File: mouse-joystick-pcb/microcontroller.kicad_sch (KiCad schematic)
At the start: 1 part

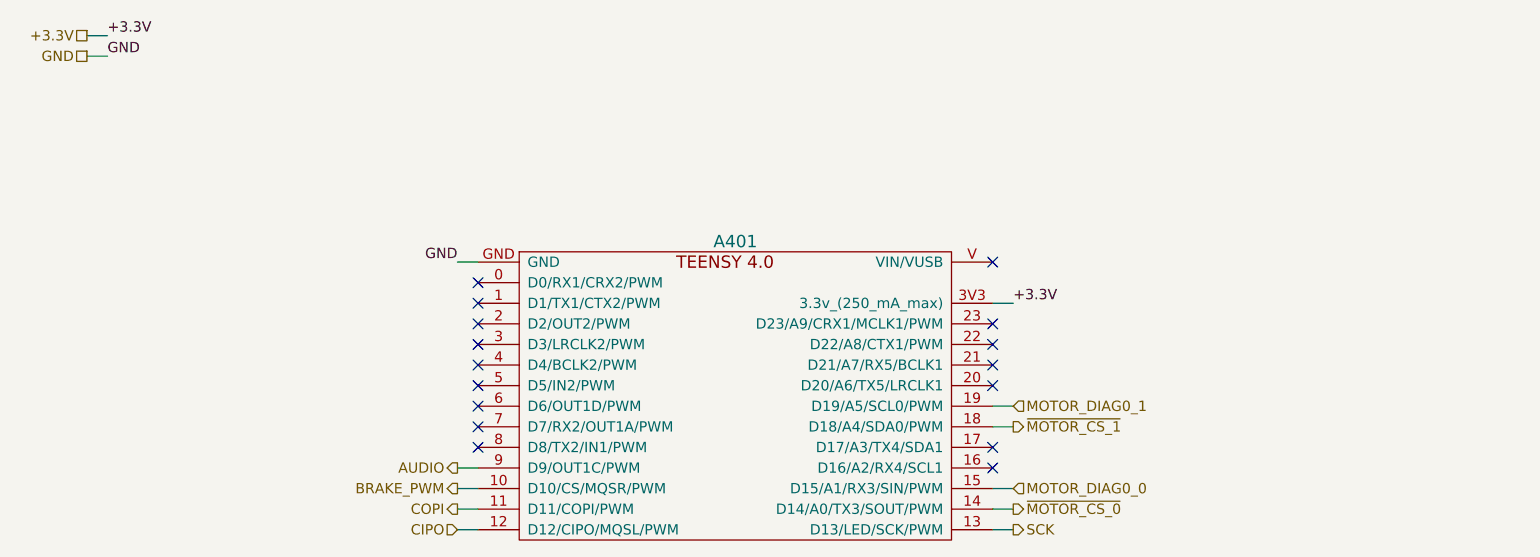
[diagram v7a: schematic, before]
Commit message: Add torque-sensor sheet
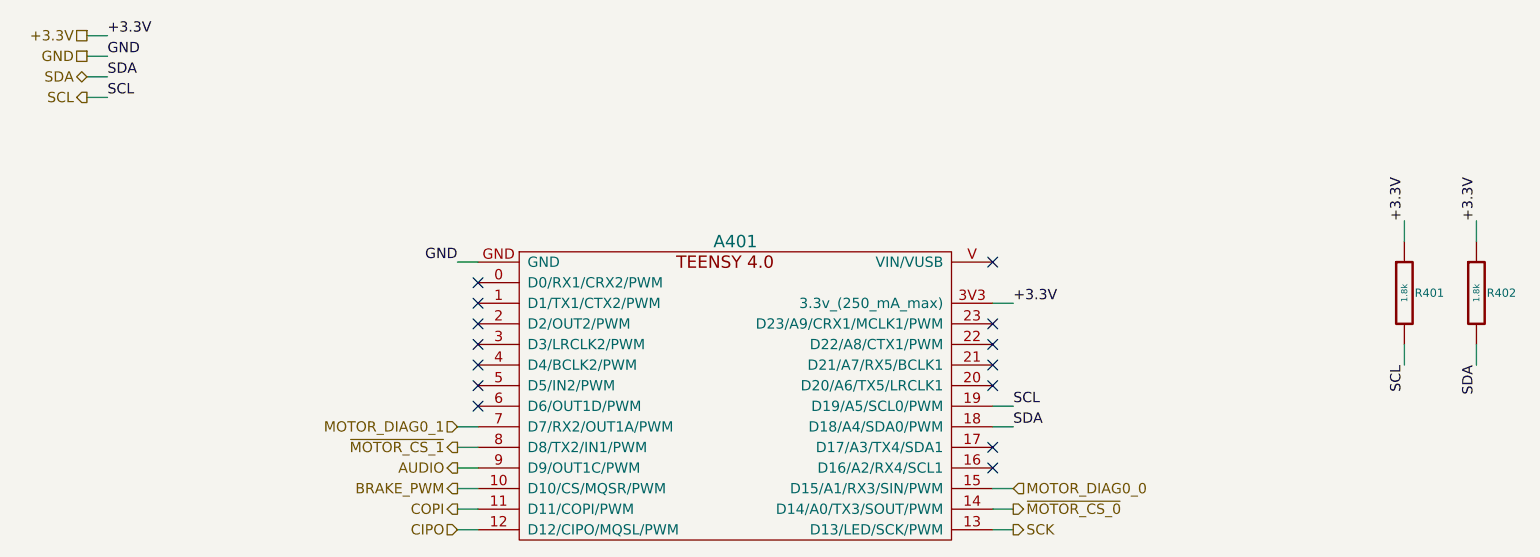
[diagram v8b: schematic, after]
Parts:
- added R401, R402: 1.8k, Janelia:R_0402_1005Metric, symbol Janelia:R_1.8k_0402
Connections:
- net +3.3V: now also R401.1, R402.1
- net MOTOR_DIAG0_1: now also A401.7 (D7/RX2/OUT1A/PWM); no longer A401.19 (D19/A5/SCL0/PWM)
- net ~{MOTOR_CS_1}: now also A401.8 (D8/TX2/IN1/PWM); no longer A401.18 (D18/A4/SDA0/PWM)
- new net SCL: A401.19 (D19/A5/SCL0/PWM), R401.2
- new net SDA: A401.18 (D18/A4/SDA0/PWM), R402.2
- no-connect marks 16 -> 14
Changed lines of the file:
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@@
   (title_block
     (title "mouse-joystick-pcb")
-    (date "2024-10-09")
+    (date "2024-10-11")
     (rev "1.0")
     (company "Peter Polidoro")
@@
   (no_connect (at 162.56 92.71))
   (no_connect (at 162.56 90.17))
-  (no_connect (at 99.06 97.79))
   (no_connect (at 99.06 85.09))
   (no_connect (at 99.06 92.71))
-  (no_connect (at 99.06 100.33))
   (no_connect (at 162.56 77.47))
   (no_connect (at 162.56 102.87))
@@
     (stroke (width 0) (type default))
   )
+  (wire (pts (xy 213.36 87.63) (xy 213.36 90.17))
+    (stroke (width 0) (type default))
+  )
+  (wire (pts (xy 50.8 57.15) (xy 53.34 57.15))
+    (stroke (width 0) (type default))
+  )
   (wire (pts (xy 99.06 102.87) (xy 96.52 102.87))
     (stroke (width 0) (type default))
@@
     (stroke (width 0) (type default))
   )
+  (wire (pts (xy 213.36 74.93) (xy 213.36 72.39))
+    (stroke (width 0) (type default))
+  )
   (wire (pts (xy 99.06 107.95) (xy 96.52 107.95))
     (stroke (width 0) (type default))
@@
     (stroke (width 0) (type default))
   )
+  (wire (pts (xy 222.25 74.93) (xy 222.25 72.39))
+    (stroke (width 0) (type default))
+  )
   (wire (pts (xy 162.56 107.95) (xy 165.1 107.95))
     (stroke (width 0) (type default))
   )
+  (wire (pts (xy 162.56 97.79) (xy 165.1 97.79))
+    (stroke (width 0) (type default))
+  )
+  (wire (pts (xy 50.8 54.61) (xy 53.34 54.61))
+    (stroke (width 0) (type default))
+  )
   (wire (pts (xy 162.56 105.41) (xy 165.1 105.41))
     (stroke (width 0) (type default))
   )
+  (wire (pts (xy 99.06 97.79) (xy 96.52 97.79))
+    (stroke (width 0) (type default))
+  )
+  (wire (pts (xy 222.25 87.63) (xy 222.25 90.17))
+    (stroke (width 0) (type default))
+  )
+  (wire (pts (xy 96.52 105.41) (xy 99.06 105.41))
+    (stroke (width 0) (type default))
+  )
+  (wire (pts (xy 99.06 77.47) (xy 96.52 77.47))
+    (stroke (width 0) (type default))
+  )
   (wire (pts (xy 162.56 95.25) (xy 165.1 95.25))
     (stroke (width 0) (type default))
   )
-  (wire (pts (xy 96.52 105.41) (xy 99.06 105.41))
-    (stroke (width 0) (type default))
-  )
-  (wire (pts (xy 99.06 77.47) (xy 96.52 77.47))
-    (stroke (width 0) (type default))
-  )
-  (wire (pts (xy 162.56 97.79) (xy 165.1 97.79))
+  (wire (pts (xy 99.06 100.33) (xy 96.52 100.33))
     (stroke (width 0) (type default))
   )
@@
     (effects (font (size 1.27 1.27)) (justify left bottom))
   )
+  (label "SCL" (at 53.34 57.15 0) (fields_autoplaced)
+    (effects (font (size 1.27 1.27)) (justify left bottom))
+  )
+  (label "SDA" (at 53.34 54.61 0) (fields_autoplaced)
+    (effects (font (size 1.27 1.27)) (justify left bottom))
+  )
   (label "GND" (at 53.34 52.07 0) (fields_autoplaced)
+    (effects (font (size 1.27 1.27)) (justify left bottom))
+  )
+  (label "+3.3V" (at 222.25 72.39 90) (fields_autoplaced)
     (effects (font (size 1.27 1.27)) (justify left bottom))
   )
@@
     (effects (font (size 1.27 1.27)) (justify right bottom))
   )
+  (label "SCL" (at 213.36 90.17 270) (fields_autoplaced)
+    (effects (font (size 1.27 1.27)) (justify right bottom))
+  )
+  (label "SDA" (at 165.1 97.79 0) (fields_autoplaced)
+    (effects (font (size 1.27 1.27)) (justify left bottom))
+  )
   (label "+3.3V" (at 53.34 49.53 0) (fields_autoplaced)
+    (effects (font (size 1.27 1.27)) (justify left bottom))
+  )
+  (label "+3.3V" (at 213.36 72.39 90) (fields_autoplaced)
+    (effects (font (size 1.27 1.27)) (justify left bottom))
+  )
+  (label "SDA" (at 222.25 90.17 270) (fields_autoplaced)
+    (effects (font (size 1.27 1.27)) (justify right bottom))
+  )
+  (label "SCL" (at 165.1 95.25 0) (fields_autoplaced)
     (effects (font (size 1.27 1.27)) (justify left bottom))
   )
@@
     (effects (font (size 1.27 1.27)) (justify right))
   )
-  (hierarchical_label "MOTOR_DIAG0_1" (shape input) (at 165.1 95.25 0) (fields_autoplaced)
-    (effects (font (size 1.27 1.27)) (justify left))
+  (hierarchical_label "MOTOR_DIAG0_1" (shape input) (at 96.52 97.79 180) (fields_autoplaced)
+    (effects (font (size 1.27 1.27)) (justify right))
+  )
+  (hierarchical_label "SCL" (shape output) (at 50.8 57.15 180) (fields_autoplaced)
+    (effects (font (size 1.27 1.27)) (justify right))
   )
   (hierarchical_label "GND" (shape passive) (at 50.8 52.07 180) (fields_autoplaced)
@@
     (effects (font (size 1.27 1.27)) (justify left))
   )
+  (hierarchical_label "SDA" (shape bidirectional) (at 50.8 54.61 180) (fields_autoplaced)
+    (effects (font (size 1.27 1.27)) (justify right))
+  )
   (hierarchical_label "AUDIO" (shape output) (at 96.52 102.87 180) (fields_autoplaced)
     (effects (font (size 1.27 1.27)) (justify right))
@@
     (effects (font (size 1.27 1.27)) (justify left))
   )
-  (hierarchical_label "~{MOTOR_CS_1}" (shape output) (at 165.1 97.79 0) (fields_autoplaced)
-    (effects (font (size 1.27 1.27)) (justify left))
+  (hierarchical_label "~{MOTOR_CS_1}" (shape output) (at 96.52 100.33 180) (fields_autoplaced)
+    (effects (font (size 1.27 1.27)) (justify right))
   )
   (hierarchical_label "COPI" (shape output) (at 96.52 107.95 180) (fields_autoplaced)
     (effects (font (size 1.27 1.27)) (justify right))
   )
+  (symbol (lib_id "Janelia:R_1.8k_0402") (at 222.25 81.28 0) (unit 1)
+    (in_bom yes) (on_board yes) (dnp no)
+    (property "Reference" "R402" (at 223.52 81.28 0)
+      (effects (font (size 1.016 1.016)) (justify left))
+    )
+    (property "Value" "1.8k" (at 222.25 81.28 90) (do_not_autoplace)
+      (effects (font (size 0.762 0.762)))
+    )
+    (property "Footprint" "Janelia:R_0402_1005Metric" (at 220.472 81.28 90)
+      (effects (font (size 0.762 0.762)) hide)
+    )
+    (property "Datasheet" "" (at 224.282 81.28 90)
+      (effects (font (size 0.762 0.762)))
+    )
+    (property "Vendor" "JLCPCB" (at 226.822 78.74 90)
+      (effects (font (size 1.524 1.524)) hide)
+    )
+    (property "Vendor Part Number" "C409855" (at 229.362 76.2 90)
+      (effects (font (size 1.524 1.524)) hide)
+    )
+    (property "Synopsis" "RES SMD 1.8K OHM 5% 100mW" (at 231.902 73.66 90)
+      (effects (font (size 1.524 1.524)) hide)
+    )
+    (property "Package" "0402" (at 222.25 81.28 0)
+      (effects (font (size 1.27 1.27)) hide)
+    )
+    (property "Manufacturer" "PANASONIC" (at 222.25 81.28 0)
+      (effects (font (size 1.27 1.27)) hide)
+    )
+    (property "Manufacturer Part Number" "ERJ2GEJ182X" (at 222.25 81.28 0)
+      (effects (font (size 1.27 1.27)) hide)
+    )
+    (property "LCSC" "C409855" (at 222.25 81.28 0)
+      (effects (font (size 1.27 1.27)) hide)
+    )
+    (pin "2")
+    (pin "1")
+    (instances
+      (project "mouse-joystick-pcb"
+        (path "/df2b2e89-e055-4140-95de-f1df723db034/90ad6836-1738-4b32-a341-0a0b169f4662"
+          (reference "R402") (unit 1)
+        )
+      )
+    )
+  )
+  (symbol (lib_id "Janelia:R_1.8k_0402") (at 213.36 81.28 0) (unit 1)
+    (in_bom yes) (on_board yes) (dnp no)
+    (property "Reference" "R401" (at 214.63 81.28 0)
+      (effects (font (size 1.016 1.016)) (justify left))
+    )
+    (property "Value" "1.8k" (at 213.36 81.28 90) (do_not_autoplace)
+      (effects (font (size 0.762 0.762)))
+    )
+    (property "Footprint" "Janelia:R_0402_1005Metric" (at 211.582 81.28 90)
+      (effects (font (size 0.762 0.762)) hide)
+    )
+    (property "Datasheet" "" (at 215.392 81.28 90)
+      (effects (font (size 0.762 0.762)))
+    )
+    (property "Vendor" "JLCPCB" (at 217.932 78.74 90)
+      (effects (font (size 1.524 1.524)) hide)
+    )
+    (property "Vendor Part Number" "C409855" (at 220.472 76.2 90)
+      (effects (font (size 1.524 1.524)) hide)
+    )
+    (property "Synopsis" "RES SMD 1.8K OHM 5% 100mW" (at 223.012 73.66 90)
+      (effects (font (size 1.524 1.524)) hide)
+    )
+    (property "Package" "0402" (at 213.36 81.28 0)
+      (effects (font (size 1.27 1.27)) hide)
+    )
+    (property "Manufacturer" "PANASONIC" (at 213.36 81.28 0)
+      (effects (font (size 1.27 1.27)) hide)
+    )
+    (property "Manufacturer Part Number" "ERJ2GEJ182X" (at 213.36 81.28 0)
+      (effects (font (size 1.27 1.27)) hide)
+    )
+    (property "LCSC" "C409855" (at 213.36 81.28 0)
+      (effects (font (size 1.27 1.27)) hide)
+    )
+    (pin "2")
+    (pin "1")
+    (instances
+      (project "mouse-joystick-pcb"
+        (path "/df2b2e89-e055-4140-95de-f1df723db034/90ad6836-1738-4b32-a341-0a0b169f4662"
+          (reference "R401") (unit 1)
+        )
+      )
+    )
+  )
   (symbol (lib_id "Janelia:TEENSY_4.0_HEADERS") (at 130.81 93.98 0) (unit 1)
